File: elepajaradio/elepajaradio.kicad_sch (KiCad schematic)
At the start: 29 parts, among them J1 SPI, J2 UART, J3 vdd_gnd, J4 reset, SW1 RotaryEncoder, SW2 SW_Push, SW3 SW_Push, U1 MAX2606, U2 OLED_I2C, U3 ATmega328PB-A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

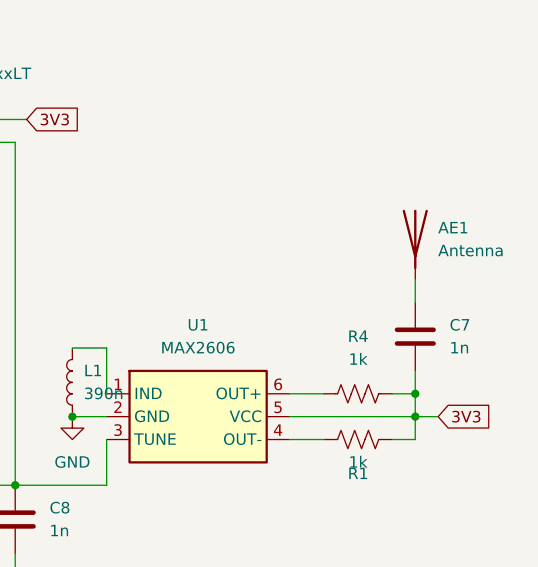
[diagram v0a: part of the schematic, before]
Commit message: fixing vco output nodes
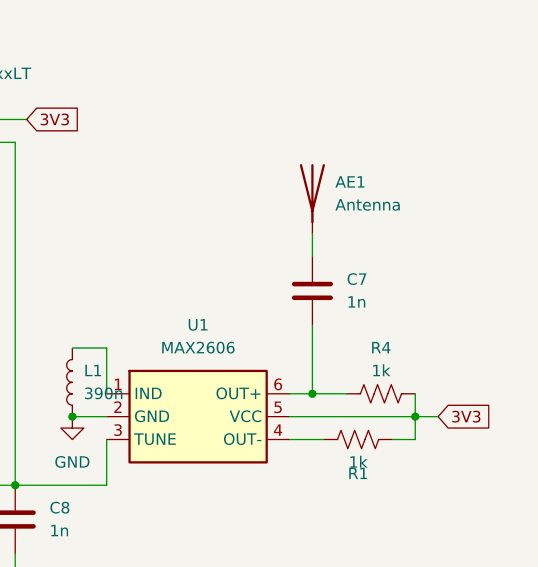
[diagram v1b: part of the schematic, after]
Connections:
- net 3V3: no longer C7.2
- net at R4.2, U1.6 (OUT+): now also C7.2
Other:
- moved on the sheet: AE1, C7, R4
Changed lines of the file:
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@@
   (junction (at 132.08 63.5) (diameter 0) (color 0 0 0 0)
   )
-  (junction (at 220.98 125.73) (diameter 0) (color 0 0 0 0)
-  )
   (junction (at 46.99 147.32) (diameter 0) (color 0 0 0 0)
   )
@@
   )
   (junction (at 39.37 147.32) (diameter 0) (color 0 0 0 0)
+  )
+  (junction (at 209.55 125.73) (diameter 0) (color 0 0 0 0)
   )
   (junction (at 156.21 135.89) (diameter 0) (color 0 0 0 0)
@@
     (stroke (width 0) (type default))
   )
-  (wire (pts (xy 220.98 123.19) (xy 220.98 125.73))
-    (stroke (width 0) (type default))
-  )
   (wire (pts (xy 176.53 97.79) (xy 173.99 97.79))
     (stroke (width 0) (type default))
@@
     (stroke (width 0) (type default))
   )
+  (wire (pts (xy 209.55 118.11) (xy 209.55 125.73))
+    (stroke (width 0) (type default))
+  )
   (wire (pts (xy 182.88 128.27) (xy 186.69 128.27))
     (stroke (width 0) (type default))
@@
     (stroke (width 0) (type default))
   )
-  (wire (pts (xy 218.44 125.73) (xy 220.98 125.73))
-    (stroke (width 0) (type default))
-  )
   (wire (pts (xy 53.34 29.21) (xy 53.34 46.99))
     (stroke (width 0) (type default))
@@
     (stroke (width 0) (type default))
   )
+  (wire (pts (xy 209.55 125.73) (xy 213.36 125.73))
+    (stroke (width 0) (type default))
+  )
   (wire (pts (xy 148.59 102.87) (xy 153.67 102.87))
     (stroke (width 0) (type default))
@@
     (stroke (width 0) (type default))
   )
-  (wire (pts (xy 220.98 113.03) (xy 220.98 115.57))
+  (wire (pts (xy 209.55 107.95) (xy 209.55 110.49))
     (stroke (width 0) (type default))
   )
@@
     (stroke (width 0) (type default))
   )
-  (wire (pts (xy 207.01 125.73) (xy 210.82 125.73))
+  (wire (pts (xy 207.01 125.73) (xy 209.55 125.73))
     (stroke (width 0) (type default))
   )
@@
     )
   )
-  (symbol (lib_id "Device:C") (at 220.98 119.38 0) (unit 1)
-    (in_bom yes) (on_board yes) (dnp no) (fields_autoplaced)
-    (property "Reference" "C7" (at 224.79 118.1099 0)
-      (effects (font (size 1.27 1.27)) (justify left))
-    )
-    (property "Value" "1n" (at 224.79 120.6499 0)
-      (effects (font (size 1.27 1.27)) (justify left))
-    )
-    (property "Footprint" "Capacitor_SMD:C_0603_1608Metric" (at 221.9452 123.19 0)
-      (effects (font (size 1.27 1.27)) hide)
-    )
-    (property "Datasheet" "~" (at 220.98 119.38 0)
+  (symbol (lib_id "Device:C") (at 209.55 114.3 0) (unit 1)
+    (in_bom yes) (on_board yes) (dnp no) (fields_autoplaced)
+    (property "Reference" "C7" (at 213.36 113.0299 0)
+      (effects (font (size 1.27 1.27)) (justify left))
+    )
+    (property "Value" "1n" (at 213.36 115.5699 0)
+      (effects (font (size 1.27 1.27)) (justify left))
+    )
+    (property "Footprint" "Capacitor_SMD:C_0603_1608Metric" (at 210.5152 118.11 0)
+      (effects (font (size 1.27 1.27)) hide)
+    )
+    (property "Datasheet" "~" (at 209.55 114.3 0)
       (effects (font (size 1.27 1.27)) hide)
     )
@@
     )
   )
-  (symbol (lib_id "Device:Antenna") (at 220.98 107.95 0) (unit 1)
-    (in_bom yes) (on_board yes) (dnp no) (fields_autoplaced)
-    (property "Reference" "AE1" (at 223.52 107.3149 0)
-      (effects (font (size 1.27 1.27)) (justify left))
-    )
-    (property "Value" "Antenna" (at 223.52 109.8549 0)
-      (effects (font (size 1.27 1.27)) (justify left))
-    )
-    (property "Footprint" "Connector_Coaxial:BNC_TEConnectivity_1478204_Vertical" (at 220.98 107.95 0)
-      (effects (font (size 1.27 1.27)) hide)
-    )
-    (property "Datasheet" "~" (at 220.98 107.95 0)
+  (symbol (lib_id "Device:Antenna") (at 209.55 102.87 0) (unit 1)
+    (in_bom yes) (on_board yes) (dnp no) (fields_autoplaced)
+    (property "Reference" "AE1" (at 212.09 102.2349 0)
+      (effects (font (size 1.27 1.27)) (justify left))
+    )
+    (property "Value" "Antenna" (at 212.09 104.7749 0)
+      (effects (font (size 1.27 1.27)) (justify left))
+    )
+    (property "Footprint" "Connector_Coaxial:BNC_TEConnectivity_1478204_Vertical" (at 209.55 102.87 0)
+      (effects (font (size 1.27 1.27)) hide)
+    )
+    (property "Datasheet" "~" (at 209.55 102.87 0)
       (effects (font (size 1.27 1.27)) hide)
     )
@@
     )
   )
-  (symbol (lib_id "Device:R_US") (at 214.63 125.73 270) (unit 1)
-    (in_bom yes) (on_board yes) (dnp no) (fields_autoplaced)
-    (property "Reference" "R4" (at 214.63 119.38 90)
-      (effects (font (size 1.27 1.27)))
-    )
-    (property "Value" "1k" (at 214.63 121.92 90)
-      (effects (font (size 1.27 1.27)))
-    )
-    (property "Footprint" "Resistor_SMD:R_0603_1608Metric" (at 214.376 126.746 90)
-      (effects (font (size 1.27 1.27)) hide)
-    )
-    (property "Datasheet" "~" (at 214.63 125.73 0)
-      (effects (font (size 1.27 1.27)) hide)
-    )
+  (symbol (lib_id "Device:R_US") (at 217.17 125.73 270) (unit 1)
+    (in_bom yes) (on_board yes) (dnp no)
+    (property "Reference" "R4" (at 217.17 120.65 90)
+      (effects (font (size 1.27 1.27)))
+    )
+    (property "Value" "1k" (at 217.17 123.19 90)
+      (effects (font (size 1.27 1.27)))
+    )
+    (property "Footprint" "Resistor_SMD:R_0603_1608Metric" (at 216.916 126.746 90)
+      (effects (font (size 1.27 1.27)) hide)
+    )
+    (property "Datasheet" "~" (at 217.17 125.73 0)
+      (effects (font (size 1.27 1.27)) hide)
+    )

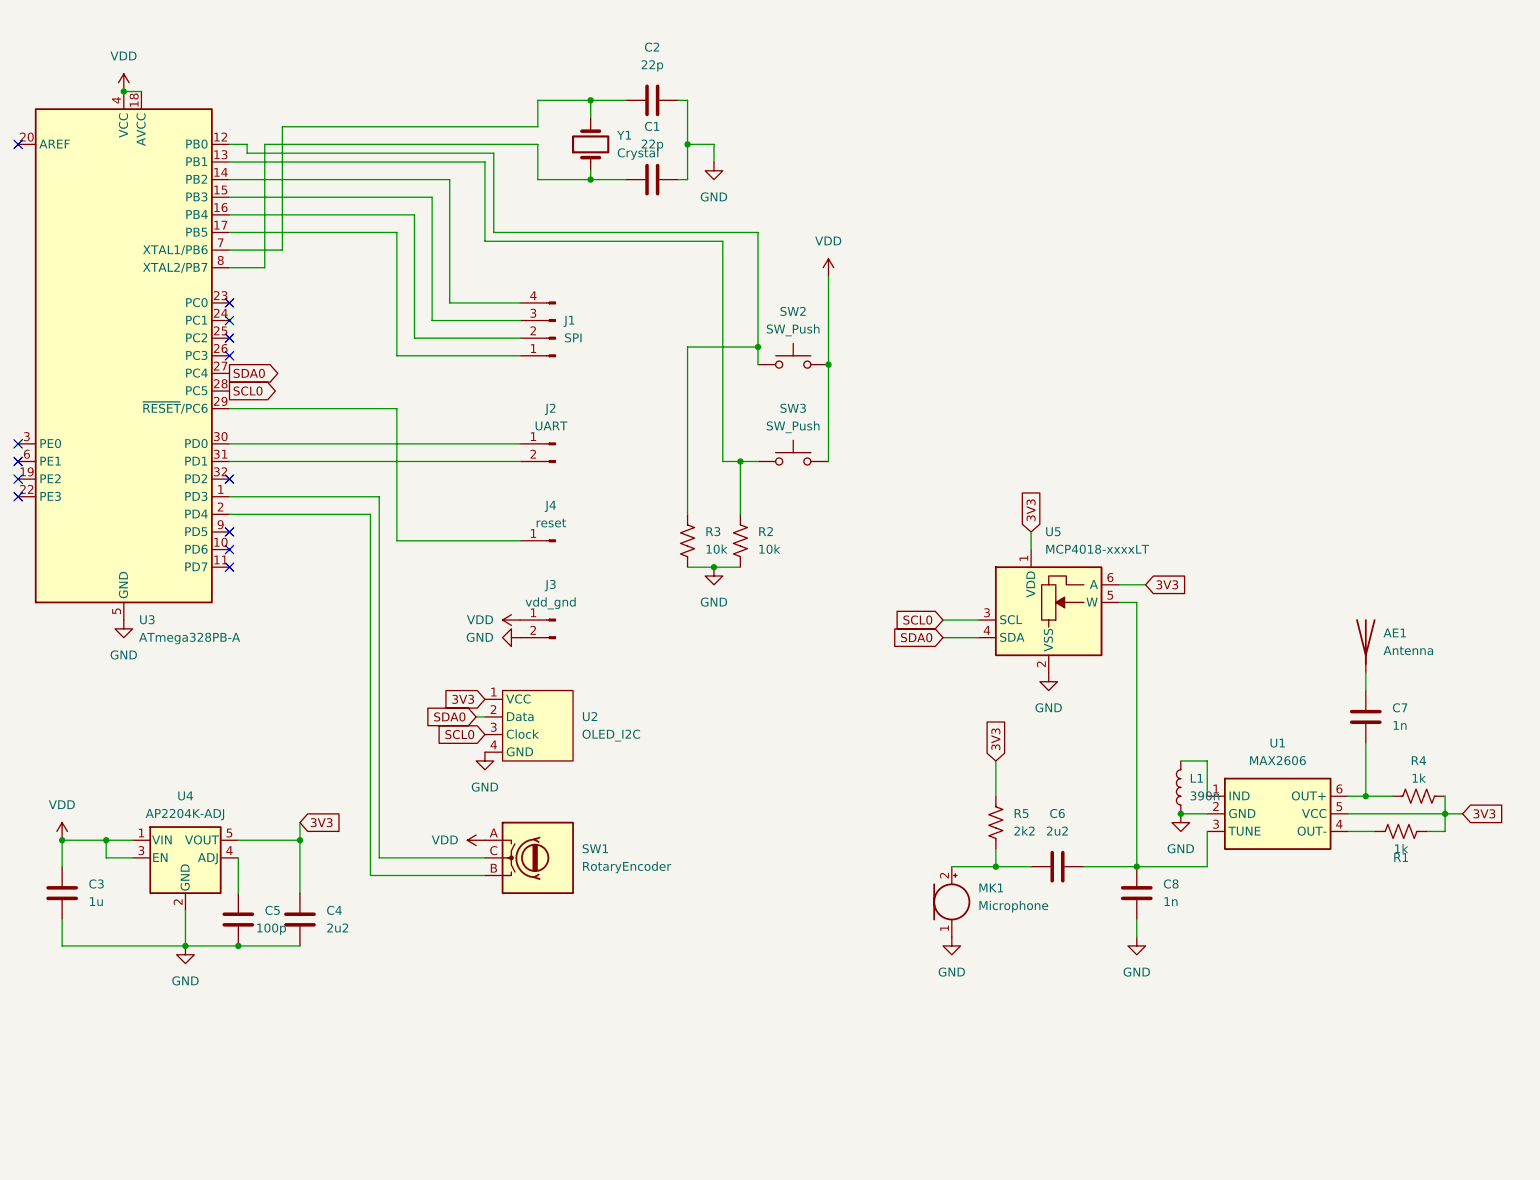
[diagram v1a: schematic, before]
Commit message: schematic updates for documentation
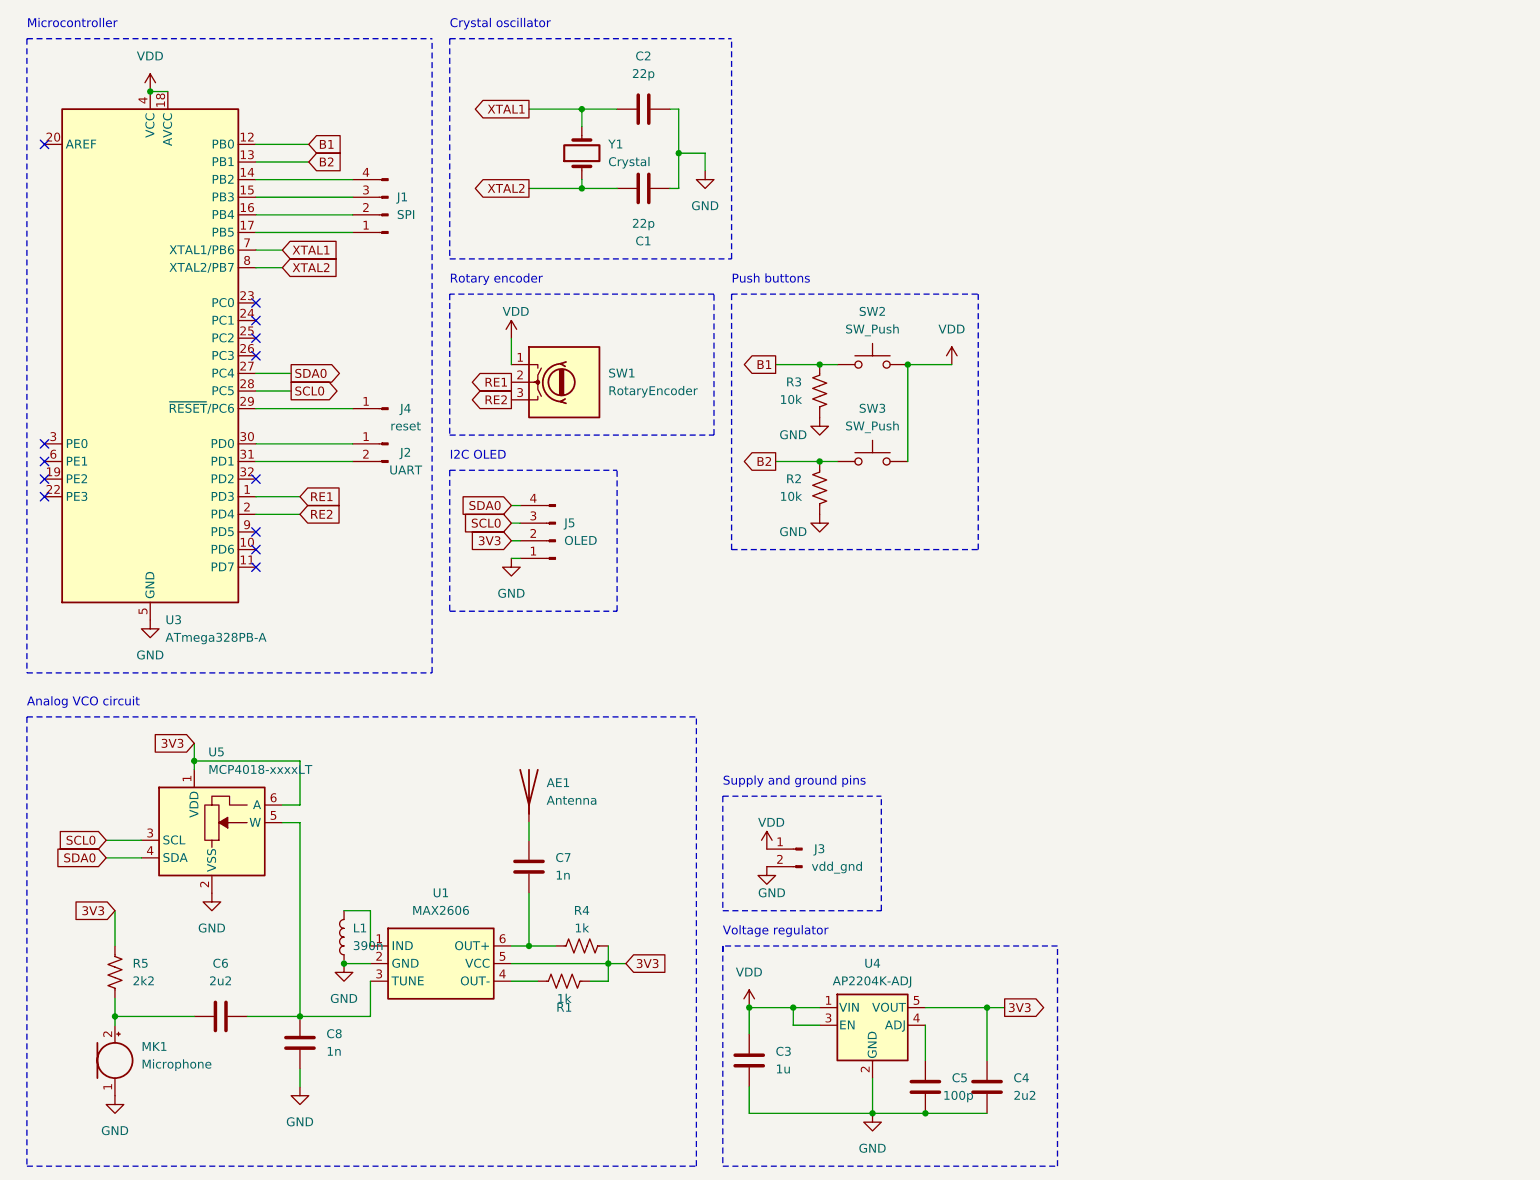
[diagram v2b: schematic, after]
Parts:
- removed U2: OLED_I2C, Connector_PinHeader_2.54mm:PinHeader_1x04_P2.54mm_Vertical, symbol oled_lafvin:OLED_I2C
- added J5: OLED, Connector_PinHeader_2.54mm:PinHeader_1x04_P2.54mm_Vertical, symbol Connector:Conn_01x04_Pin
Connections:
- net 3V3: now also J5.2 (Pin_2)
- net GND: now also J5.1 (Pin_1)
- net SCL0: now also J5.3 (Pin_3)
- net SDA0: now also J5.4 (Pin_4)
- net VDD: now also SW1.1; no longer SW1.A
- net XTAL2: now reaches C1.1, U3.8 (XTAL2/PB7), Y1.1
- net XTAL1: now reaches C2.1, U3.7 (XTAL1/PB6), Y1.2
- net RE2: now reaches U3.2 (PD4)
- net RE2: now also SW1.3; no longer SW1.B
- net RE1: now reaches U3.1 (PD3)
- net RE1: now also SW1.2; no longer SW1.C
- net B2: now reaches R2.2, SW3.1, U3.13 (PB1)
- net B1: now reaches R3.2, SW2.1, U3.12 (PB0)
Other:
- note added: "Analog VCO circuit"
- note added: "Crystal oscillator"
- note added: "I2C OLED"
- note added: "Microcontroller"
- note added: "Push buttons"
- note added: "Rotary encoder"
- note added: "Supply and ground pins"
- note added: "Voltage regulator"
- moved on the sheet: AE1, C1, C2, C3, C4, C5, C6, C7, C8, J1, J2, J3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

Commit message: updates for second order
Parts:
- AE1: footprint Connector_Coaxial:BNC_TEConnectivity_1478204_Vertical -> Connector_Coaxial:SMA_Amphenol_901-143_Horizontal
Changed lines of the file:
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@@
       (effects (font (size 1.27 1.27)) (justify left))
     )
-    (property "Footprint" "Connector_Coaxial:BNC_TEConnectivity_1478204_Vertical" (at 88.9 124.46 0)
+    (property "Footprint" "Connector_Coaxial:SMA_Amphenol_901-143_Horizontal" (at 88.9 124.46 0)
       (effects (font (size 1.27 1.27)) hide)
     )
